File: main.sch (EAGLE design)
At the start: 41 parts

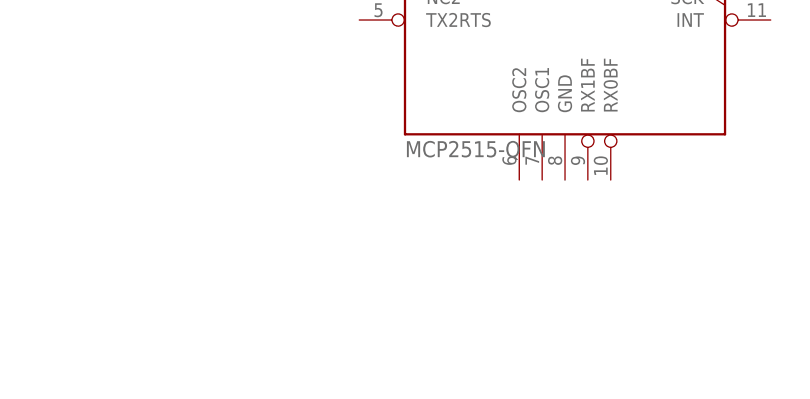
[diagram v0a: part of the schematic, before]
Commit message: added 0402 capacitor
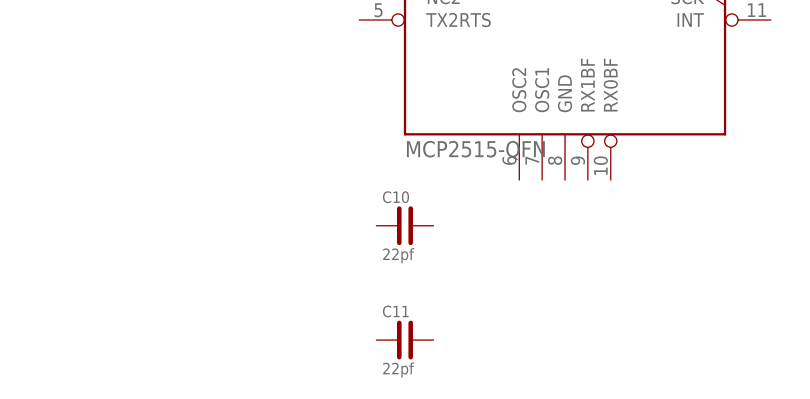
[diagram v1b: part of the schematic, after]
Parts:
- added C10, C11: 22pf, SamuelLibrary:0402_CAPACITOR
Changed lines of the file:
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@@
 <part name="SUPPLY10" library="supply2" library_urn="urn:adsk.eagle:library:372" deviceset="GND" device=""/>
 <part name="+3V10" library="supply1" library_urn="urn:adsk.eagle:library:371" deviceset="+3V3" device=""/>
+<part name="C10" library="SamuelLibrary" deviceset="0402_CAPACITOR" device="" package3d_urn="urn:adsk.eagle:package:28904593/1" value="22pf"/>
+<part name="C11" library="SamuelLibrary" deviceset="0402_CAPACITOR" device="" package3d_urn="urn:adsk.eagle:package:28904593/1" value="22pf"/>
 </parts>
 <sheets>
@@
 <attribute name="VALUE" x="287.02" y="228.6" size="1.778" layer="96" rot="R90"/>
 </instance>
+<instance part="C10" gate="G$1" x="68.58" y="25.4" smashed="yes">
+<attribute name="NAME" x="66.04" y="27.94" size="1.27" layer="95"/>
+<attribute name="VALUE" x="66.04" y="21.59" size="1.27" layer="96"/>
+</instance>
+<instance part="C11" gate="G$1" x="68.58" y="12.7" smashed="yes">
+<attribute name="NAME" x="66.04" y="15.24" size="1.27" layer="95"/>
+<attribute name="VALUE" x="66.04" y="8.89" size="1.27" layer="96"/>
+</instance>
 </instances>

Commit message: can interface and data sheets
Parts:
- removed C10, C11: 22pf, SamuelLibrary:0402_CAPACITOR
- removed R1, R10, R11, R12, R13, R14, R15, R16, R17, R18, R19, R2, R20, R3, R4, R5, R6, R7, R8, R9: 20k, Resistors:1-2176053-4
- added C8, C9: 22p, SamuelLibrary:0402_CAPACITOR
- added MCP2515: MCP2515-QFN, SamuelLibrary:MCP2515-QFN
- added U$1: 10k, SamuelLibrary:1206_RESISTOR
- added U$10, U$11, U$12, U$13, U$14, U$15, U$16, U$17, U$18, U$19, U$2, U$20, U$21, U$3, U$5, U$6, U$7, U$8, U$9: 20k, SamuelLibrary:0805_RESISTOR
- added U$22: 120, SamuelLibrary:0603_RESISTOR
- added U$23: 1k, SamuelLibrary:1206_RESISTOR
- added U$24: SN65HVD230Q, SamuelLibrary:SN65HVD230Q
- added U$25: ADC124S051, SamuelLibrary:ADC124S051
- added XTAL1: 8M, SamuelLibrary:CRYSTAL
- U$4: value MCP2515-QFN -> 20k; device SamuelLibrary:MCP2515-QFN -> SamuelLibrary:0805_RESISTOR
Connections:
- net N$17 renamed CE1
- net N$36 renamed SPI_SCK
- removed net N$45: R15.1, R16.2
- removed net N$47: R17.1, R18.2
- removed net N$49: R19.1, R20.2
- new net CAN_RX: MCP2515.RXCAN, U$24.R
- new net CAN_TX: MCP2515.TXCAN, U$24.D
- new net CE0: GPIO.23, MCP2515.CS
- new net N$17: U$12.P$2, U$13.P$1
- new net N$20: C8.L2, MCP2515.OSC2, XTAL1.L1
- new net N$36: U$23.P$1, U$24.S
- new net N$41: C9.L2, MCP2515.OSC1, XTAL1.L2
- new net N$48: MCP2515.RESET, U$1.P$2
- new net SCK: MCP2515.SCK
- new net SPI_MISO: GPIO.20, MCP2515.SO
- new net SPI_MOSI: GPIO.22, MCP2515.SI
- new net ~INT: GPIO.21, MCP2515.INT
- net +3V3: now also GPIO.18, MCP2515.VDD, U$1.P$1, U$10.P$1, U$12.P$1, U$14.P$1, U$16.P$1, U$2.P$1, U$24.VCC, U$4.P$1, U$6.P$1, U$8.P$1; no longer R1.2, R11.2, R13.2, R15.2, R3.2, R5.2, R7.2, R9.2
- net GND: now also C8.L1, C9.L1, MCP2515.GND, U$18.P$1, U$20.P$1, U$23.P$2, U$24.GND, U$25.GND; no longer R18.1, R20.1
- net N$11: now also U$4.P$2, U$5.P$1; no longer R3.1, R4.2
- net N$14: now also U$6.P$2, U$7.P$1; no longer R5.1, R6.2
- net N$15: now also U$8.P$2, U$9.P$1; no longer GPIO.21
- net N$16: now also U$10.P$2, U$11.P$1; no longer GPIO.23
- net N$18: now also U$7.P$2; no longer R10.1
- net N$19: now also U$9.P$2; no longer R14.1
- net N$21: now also U$14.P$2, U$15.P$1; no longer R7.1, R8.2
- net N$25: now also U$16.P$2, U$17.P$1; no longer R10.2, R9.1
- net N$26: now also U$17.P$2; no longer R16.1
- net N$27: now also U$18.P$2, U$19.P$1; no longer R11.1, R12.2
- net N$33: now also U$20.P$2, U$21.P$1; no longer GPIO.18
- net N$34: now also U$22.P$2, U$24.CANH; no longer GPIO.20
- net N$35: now also U$22.P$1, U$24.CANL; no longer GPIO.22
- net N$37: now also U$15.P$2; no longer R12.1
- net N$38: now also U$25.VA; no longer R13.1, R14.2
- net N$44: now also U$13.P$2; no longer R8.1
- net N$46: now also U$11.P$2; no longer R4.1
- net N$5: now also U$3.P$2; no longer R2.1
- net N$6: now also U$2.P$2, U$3.P$1; no longer R1.1, R2.2
- net N$7: now also U$5.P$2; no longer R6.1
- net PWM0: now also U$19.P$2; no longer R17.2
- net PWM1: now also U$21.P$2; no longer R19.2

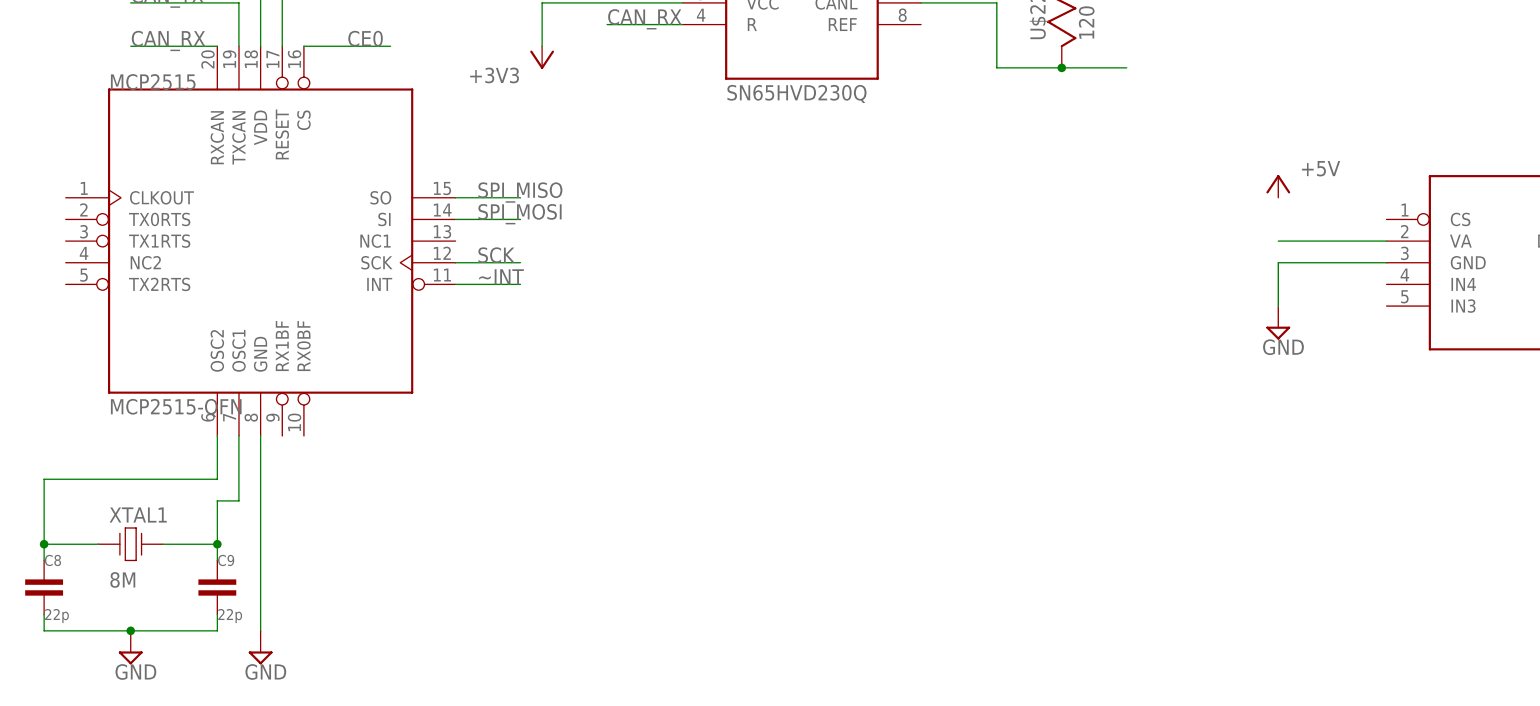
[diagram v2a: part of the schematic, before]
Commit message: adc power supply
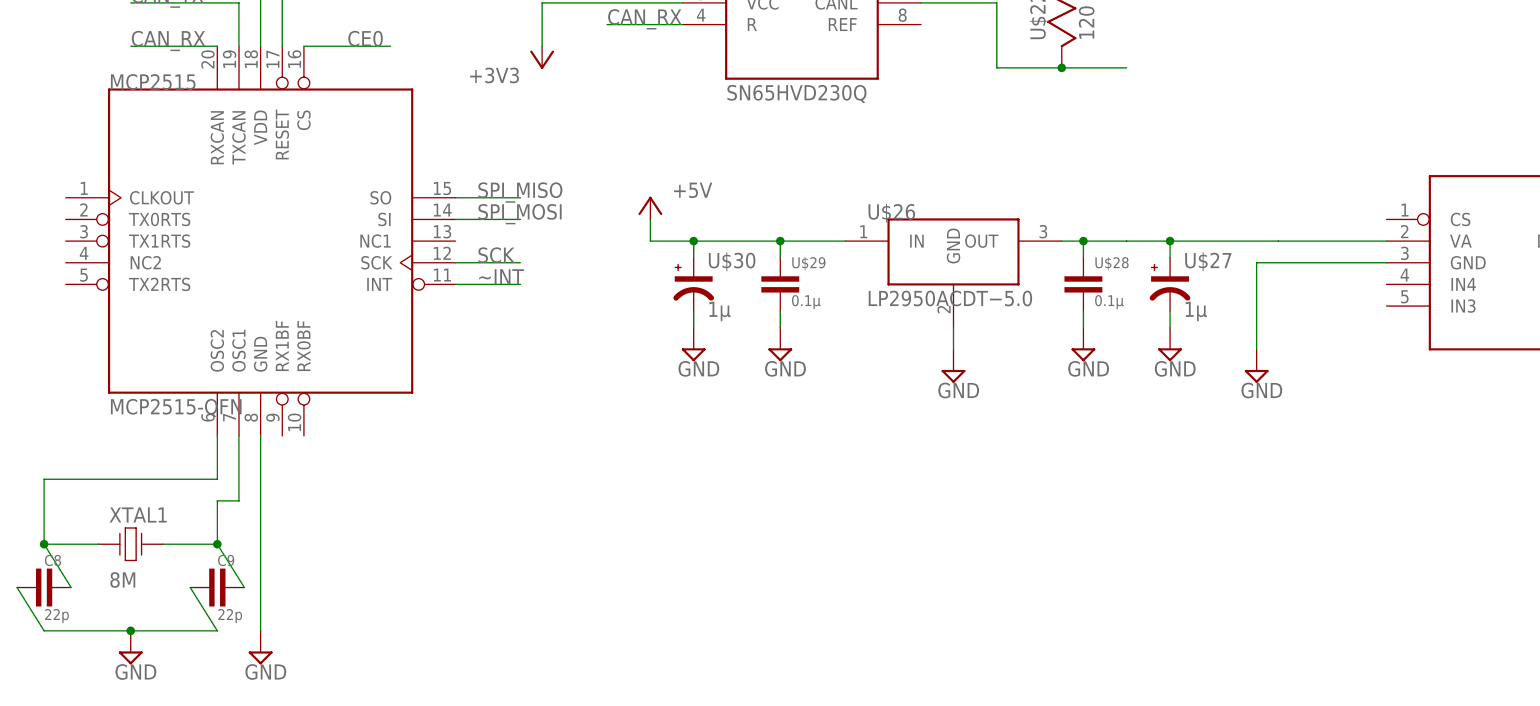
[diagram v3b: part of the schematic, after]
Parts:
- added U$26: LP2950ACDT−5.0, SamuelLibrary:LP2950ACDT−5.0
- added U$27, U$30: 1µ, SamuelLibrary:1206_POL_TANT_CAP
- added U$28, U$29: 0.1µ, SamuelLibrary:0603_CAPACITOR
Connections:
- net +5V: now also U$26.IN, U$29.L1, U$30.P$1
- net GND: now also U$26.GND, U$27.P$2, U$28.L2, U$29.L2, U$30.P$2
- net N$38: now also U$26.OUT, U$27.P$1, U$28.L1
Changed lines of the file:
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@@
 <part name="SUPPLY23" library="supply2" library_urn="urn:adsk.eagle:library:372" deviceset="GND" device=""/>
 <part name="P+10" library="supply1" library_urn="urn:adsk.eagle:library:371" deviceset="+5V" device=""/>
+<part name="U$26" library="SamuelLibrary" deviceset="LP2950ACDT−5.0" device="" package3d_urn="urn:adsk.eagle:package:28946626/1"/>
+<part name="U$27" library="SamuelLibrary" deviceset="1206_POL_TANT_CAP" device="" package3d_urn="urn:adsk.eagle:package:28960391/1" value="1µ"/>
+<part name="U$28" library="SamuelLibrary" deviceset="0603_CAPACITOR" device="" package3d_urn="urn:adsk.eagle:package:28960470/1" value="0.1µ"/>
+<part name="U$29" library="SamuelLibrary" deviceset="0603_CAPACITOR" device="" package3d_urn="urn:adsk.eagle:package:28960470/1" value="0.1µ"/>
+<part name="U$30" library="SamuelLibrary" deviceset="1206_POL_TANT_CAP" device="" package3d_urn="urn:adsk.eagle:package:28960391/1" value="1µ"/>
+<part name="SUPPLY24" library="supply2" library_urn="urn:adsk.eagle:library:372" deviceset="GND" device=""/>
+<part name="SUPPLY25" library="supply2" library_urn="urn:adsk.eagle:library:372" deviceset="GND" device=""/>
+<part name="SUPPLY26" library="supply2" library_urn="urn:adsk.eagle:library:372" deviceset="GND" device=""/>
+<part name="SUPPLY27" library="supply2" library_urn="urn:adsk.eagle:library:372" deviceset="GND" device=""/>
+<part name="SUPPLY28" library="supply2" library_urn="urn:adsk.eagle:library:372" deviceset="GND" device=""/>
 </parts>
 <sheets>
@@
 </instance>
 <instance part="U$25" gate="G$1" x="187.96" y="60.96" smashed="yes"/>
-<instance part="SUPPLY23" gate="GND" x="160.02" y="53.34" smashed="yes">
-<attribute name="VALUE" x="158.115" y="50.165" size="1.778" layer="96"/>
-</instance>
-<instance part="P+10" gate="1" x="160.02" y="71.12" smashed="yes">
-<attribute name="VALUE" x="162.56" y="71.12" size="1.778" layer="96"/>
+<instance part="SUPPLY23" gate="GND" x="157.48" y="48.26" smashed="yes">
+<attribute name="VALUE" x="155.575" y="45.085" size="1.778" layer="96"/>
+</instance>
+<instance part="P+10" gate="1" x="86.36" y="68.58" smashed="yes">
+<attribute name="VALUE" x="88.9" y="68.58" size="1.778" layer="96"/>
+</instance>
+<instance part="U$26" gate="G$1" x="121.92" y="63.5" smashed="yes">
+<attribute name="NAME" x="111.76" y="66.04" size="1.778" layer="95"/>
+<attribute name="VALUE" x="111.76" y="55.88" size="1.778" layer="96"/>
+</instance>
+<instance part="U$27" gate="G$1" x="147.32" y="58.42" smashed="yes">
+<attribute name="NAME" x="148.9075" y="60.325" size="1.778" layer="95"/>
+<attribute name="VALUE" x="148.9075" y="54.61" size="1.778" layer="96"/>
+</instance>
+<instance part="U$28" gate="G$1" x="137.16" y="58.42" smashed="yes">
+<attribute name="NAME" x="138.43" y="60.325" size="1.27" layer="95"/>
+<attribute name="VALUE" x="138.43" y="55.88" size="1.27" layer="96"/>
+</instance>
+<instance part="U$29" gate="G$1" x="101.6" y="58.42" smashed="yes">
+<attribute name="NAME" x="102.87" y="60.325" size="1.27" layer="95"/>
+<attribute name="VALUE" x="102.87" y="55.88" size="1.27" layer="96"/>
+</instance>
+<instance part="U$30" gate="G$1" x="91.44" y="58.42" smashed="yes">
+<attribute name="NAME" x="93.0275" y="60.325" size="1.778" layer="95"/>
+<attribute name="VALUE" x="93.0275" y="54.61" size="1.778" layer="96"/>
+</instance>
+<instance part="SUPPLY24" gate="GND" x="147.32" y="50.8" smashed="yes">
+<attribute name="VALUE" x="145.415" y="47.625" size="1.778" layer="96"/>
+</instance>
+<instance part="SUPPLY25" gate="GND" x="137.16" y="50.8" smashed="yes">
+<attribute name="VALUE" x="135.255" y="47.625" size="1.778" layer="96"/>
+</instance>
+<instance part="SUPPLY26" gate="GND" x="101.6" y="50.8" smashed="yes">
+<attribute name="VALUE" x="99.695" y="47.625" size="1.778" layer="96"/>
+</instance>
+<instance part="SUPPLY27" gate="GND" x="91.44" y="50.8" smashed="yes">
+<attribute name="VALUE" x="89.535" y="47.625" size="1.778" layer="96"/>
+</instance>
+<instance part="SUPPLY28" gate="GND" x="121.92" y="48.26" smashed="yes">
+<attribute name="VALUE" x="120.015" y="45.085" size="1.778" layer="96"/>
 </instance>
 </instances>
@@
 </segment>
 <segment>
-<wire x1="15.24" y1="19.685" x2="15.24" y2="17.78" width="0.1524" layer="91"/>
+<wire x1="12.065" y1="22.86" x2="15.24" y2="17.78" width="0.1524" layer="91"/>
 <wire x1="15.24" y1="17.78" x2="25.4" y2="17.78" width="0.1524" layer="91"/>
 <wire x1="25.4" y1="17.78" x2="35.56" y2="17.78" width="0.1524" layer="91"/>
-<wire x1="35.56" y1="17.78" x2="35.56" y2="19.685" width="0.1524" layer="91"/>
+<wire x1="35.56" y1="17.78" x2="32.385" y2="22.86" width="0.1524" layer="91"/>
 <pinref part="SUPPLY11" gate="GND" pin="GND"/>
 <junction x="25.4" y="17.78"/>
@@
 <segment>
 <pinref part="U$25" gate="G$1" pin="GND"/>
-<wire x1="172.72" y1="60.96" x2="160.02" y2="60.96" width="0.1524" layer="91"/>
-<wire x1="160.02" y1="60.96" x2="160.02" y2="55.88" width="0.1524" layer="91"/>
+<wire x1="172.72" y1="60.96" x2="157.48" y2="60.96" width="0.1524" layer="91"/>
+<wire x1="157.48" y1="60.96" x2="157.48" y2="50.8" width="0.1524" layer="91"/>
 <pinref part="SUPPLY23" gate="GND" pin="GND"/>
+</segment>
+<segment>
+<pinref part="U$26" gate="G$1" pin="GND"/>
+<wire x1="121.92" y1="53.34" x2="121.92" y2="50.8" width="0.1524" layer="91"/>
+<pinref part="SUPPLY28" gate="GND" pin="GND"/>
+</segment>
+<segment>
+<pinref part="U$27" gate="G$1" pin="P$2"/>
+<pinref part="SUPPLY24" gate="GND" pin="GND"/>
+<wire x1="147.32" y1="55.245" x2="147.32" y2="53.34" width="0.1524" layer="91"/>
+</segment>
+<segment>
+<pinref part="U$30" gate="G$1" pin="P$2"/>
+<pinref part="SUPPLY27" gate="GND" pin="GND"/>
+<wire x1="91.44" y1="55.245" x2="91.44" y2="53.34" width="0.1524" layer="91"/>
+</segment>
+<segment>
+<pinref part="U$29" gate="G$1" pin="L2"/>
+<pinref part="SUPPLY26" gate="GND" pin="GND"/>
+<wire x1="101.6" y1="55.245" x2="101.6" y2="53.34" width="0.1524" layer="91"/>
+</segment>
+<segment>
+<pinref part="U$28" gate="G$1" pin="L2"/>
+<pinref part="SUPPLY25" gate="GND" pin="GND"/>
+<wire x1="137.16" y1="55.245" x2="137.16" y2="53.34" width="0.1524" layer="91"/>
 </segment>
 </net>
@@
 <pinref part="P+9" gate="1" pin="+5V"/>
 </segment>
+<segment>
+<pinref part="U$26" gate="G$1" pin="IN"/>
+<wire x1="109.22" y1="63.5" x2="101.6" y2="63.5" width="0.1524" layer="91"/>
+<wire x1="101.6" y1="63.5" x2="91.44" y2="63.5" width="0.1524" layer="91"/>
+<wire x1="91.44" y1="63.5" x2="86.36" y2="63.5" width="0.1524" layer="91"/>
+<wire x1="86.36" y1="63.5" x2="86.36" y2="66.04" width="0.1524" layer="91"/>
+<pinref part="P+10" gate="1" pin="+5V"/>
+<pinref part="U$30" gate="G$1" pin="P$1"/>
+<wire x1="91.44" y1="63.5" x2="91.44" y2="61.595" width="0.1524" layer="91"/>
+<junction x="91.44" y="63.5"/>
+<pinref part="U$29" gate="G$1" pin="L1"/>
+<wire x1="101.6" y1="63.5" x2="101.6" y2="61.595" width="0.1524" layer="91"/>
+<junction x="101.6" y="63.5"/>
+</segment>
 </net>
 <net name="PWM0" class="0">
@@
 <wire x1="35.56" y1="35.56" x2="15.24" y2="35.56" width="0.1524" layer="91"/>
 <wire x1="15.24" y1="35.56" x2="15.24" y2="27.94" width="0.1524" layer="91"/>
-<wire x1="15.24" y1="27.94" x2="15.24" y2="26.035" width="0.1524" layer="91"/>
+<wire x1="15.24" y1="27.94" x2="18.415" y2="22.86" width="0.1524" layer="91"/>
 <wire x1="21.59" y1="27.94" x2="15.24" y2="27.94" width="0.1524" layer="91"/>
 <junction x="15.24" y="27.94"/>
@@
 <net name="N$41" class="0">
 <segment>
-<wire x1="35.56" y1="27.94" x2="35.56" y2="26.035" width="0.1524" layer="91"/>
+<wire x1="35.56" y1="27.94" x2="38.735" y2="22.86" width="0.1524" layer="91"/>
 <wire x1="35.56" y1="27.94" x2="29.21" y2="27.94" width="0.1524" layer="91"/>
 <pinref part="MCP2515" gate="G$1" pin="OSC1"/>
@@
 <pinref part="U$25" gate="G$1" pin="VA"/>
 <wire x1="172.72" y1="63.5" x2="160.02" y2="63.5" width="0.1524" layer="91"/>
-</segment>
-</net>
+<wire x1="160.02" y1="63.5" x2="147.32" y2="63.5" width="0.1524" layer="91"/>
+<pinref part="U$27" gate="G$1" pin="P$1"/>
+<wire x1="147.32" y1="63.5" x2="147.32" y2="61.595" width="0.1524" layer="91"/>
+<wire x1="147.32" y1="63.5" x2="142.24" y2="63.5" width="0.1524" layer="91"/>
+<junction x="147.32" y="63.5"/>
+<wire x1="142.24" y1="63.5" x2="137.16" y2="63.5" width="0.1524" layer="91"/>
+<pinref part="U$26" gate="G$1" pin="OUT"/>
+<pinref part="U$28" gate="G$1" pin="L1"/>
+<wire x1="137.16" y1="63.5" x2="134.62" y2="63.5" width="0.1524" layer="91"/>
+<wire x1="137.16" y1="61.595" x2="137.16" y2="63.5" width="0.1524" layer="91"/>
+<junction x="137.16" y="63.5"/>
+</segment>
+</net>

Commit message: adc and pwr
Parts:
- removed BUCK1: MP2331HGTL-P, DogeBoardLib:MP2331HGTL-P
- removed C1: 22µ, capacitor-wima:C2.5/2
- removed C2: 0.1µ, capacitor-wima:C2.5/2
- removed C3: 1µ, capacitor-wima:C2.5/2
- removed C4: 6.8n, capacitor-wima:C2.5/2
- removed C7: 1n, capacitor-wima:C2.5/2
- removed R23: 20, rcl:R-EU_R0603
- removed R24: 604k, rcl:R-EU_R0603
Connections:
- removed net EN: BUCK1.EN, R24.1
- removed net N$1: BUCK1.BST, R23.2
- removed net N$2: BUCK1.PG, C7.2
- removed net N$3: C3.1, R23.1
- removed net N$4: BUCK1.SS, C4.1
- removed net VBATT+: BUCK1.IN, C1.1, C2.1, R24.2
- new net AI1: U$25.IN1
- new net AI2: U$25.IN2
- new net AI3: U$25.IN3
- new net AI4: U$25.IN4
- new net ANA_CS: U$25.CS
- new net ANA_DIN: U$25.DIN
- new net ANA_DOUT: U$25.DOUT
- new net ANA_SCLK: U$25.SCLK
- net GND: no longer BUCK1.GND, C1.2, C2.2, C4.2, C7.1
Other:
- note added: "PWR"
- moved on the sheet: U$26, U$27, U$28, U$29, U$30
